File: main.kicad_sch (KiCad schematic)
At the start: 80 parts, among them SW1 Kailh-Choc, SW10 Kailh-Choc, SW11 Kailh-Choc, SW12 Kailh-Choc, SW13 Kailh-Choc, SW14 Kailh-Choc, SW15 Kailh-Choc, SW16 Kailh-Choc, SW17 Kailh-Choc, SW18 Kailh-Choc, SW19 Kailh-Choc, SW2 Kailh-Choc, SW20 Kailh-Choc, SW21 Kailh-Choc, SW22 Kailh-Choc, SW23 Kailh-Choc, SW24 Kailh-Choc, SW25 Kailh-Choc, SW26 Kailh-Choc, SW27 Kailh-Choc, SW28 Kailh-Choc, SW29 Kailh-Choc, SW3 Kailh-Choc, SW30 Kailh-Choc, SW31 Kailh-Choc, SW32 Kailh-Choc, SW33 Kailh-Choc, SW34 Kailh-Choc, SW4 Kailh-Choc, SW5 Kailh-Choc, SW6 Kailh-Choc, SW7 Kailh-Choc, SW8 Kailh-Choc, SW9 Kailh-Choc, U1 nice_nano, U2 nice_nano

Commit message: Use local library only
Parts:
- Bat+0, Bat+1, BatGND0, BatGND1: footprint * duckyb-collection:1pin_conn -> urchin-footprints:1pin_Battery
- D1, D10, D11, D12, D13, D14, D15, D16, D17, D18, D19, D2, D20, D21, D22, D23, D24, D25, D26, D27, D28, D29, D3, D30, D31, D32, D33, D34, D4, D5, D6, D7, D8, D9: footprint * duckyb-collection:D_SMD_TH -> urchin-footprints:SMD_Diode_Tiny
- Display1, Display2: footprint * duckyb-collection:nice_view -> urchin-footprints:nice_view
- RSW0, RSW1: footprint * duckyb-collection:SW_RESET -> urchin-footprints:SW_RESET
- SW1, SW10, SW11, SW12, SW13, SW14, SW15, SW16, SW17, SW18, SW19, SW2, SW20, SW21, SW22, SW23, SW24, SW25, SW26, SW27, SW28, SW29, SW3, SW30, SW31, SW32, SW33, SW34, SW4, SW5, SW6, SW7, SW8, SW9: footprint * duckyb-collection:SW_Hotswap_Kailh_Choc_V1_tweaked -> urchin-footprints:SW_Hotswap_Kailh_Choc_V1_tweaked
- SW_POWER0, SW_POWER1: footprint * duckyb-collection:SPDT_C128955 -> urchin-footprints:smt-slider-switch
- U1, U2: footprint * duckyb-collection:nice_nano -> urchin-footprints:nice_nano

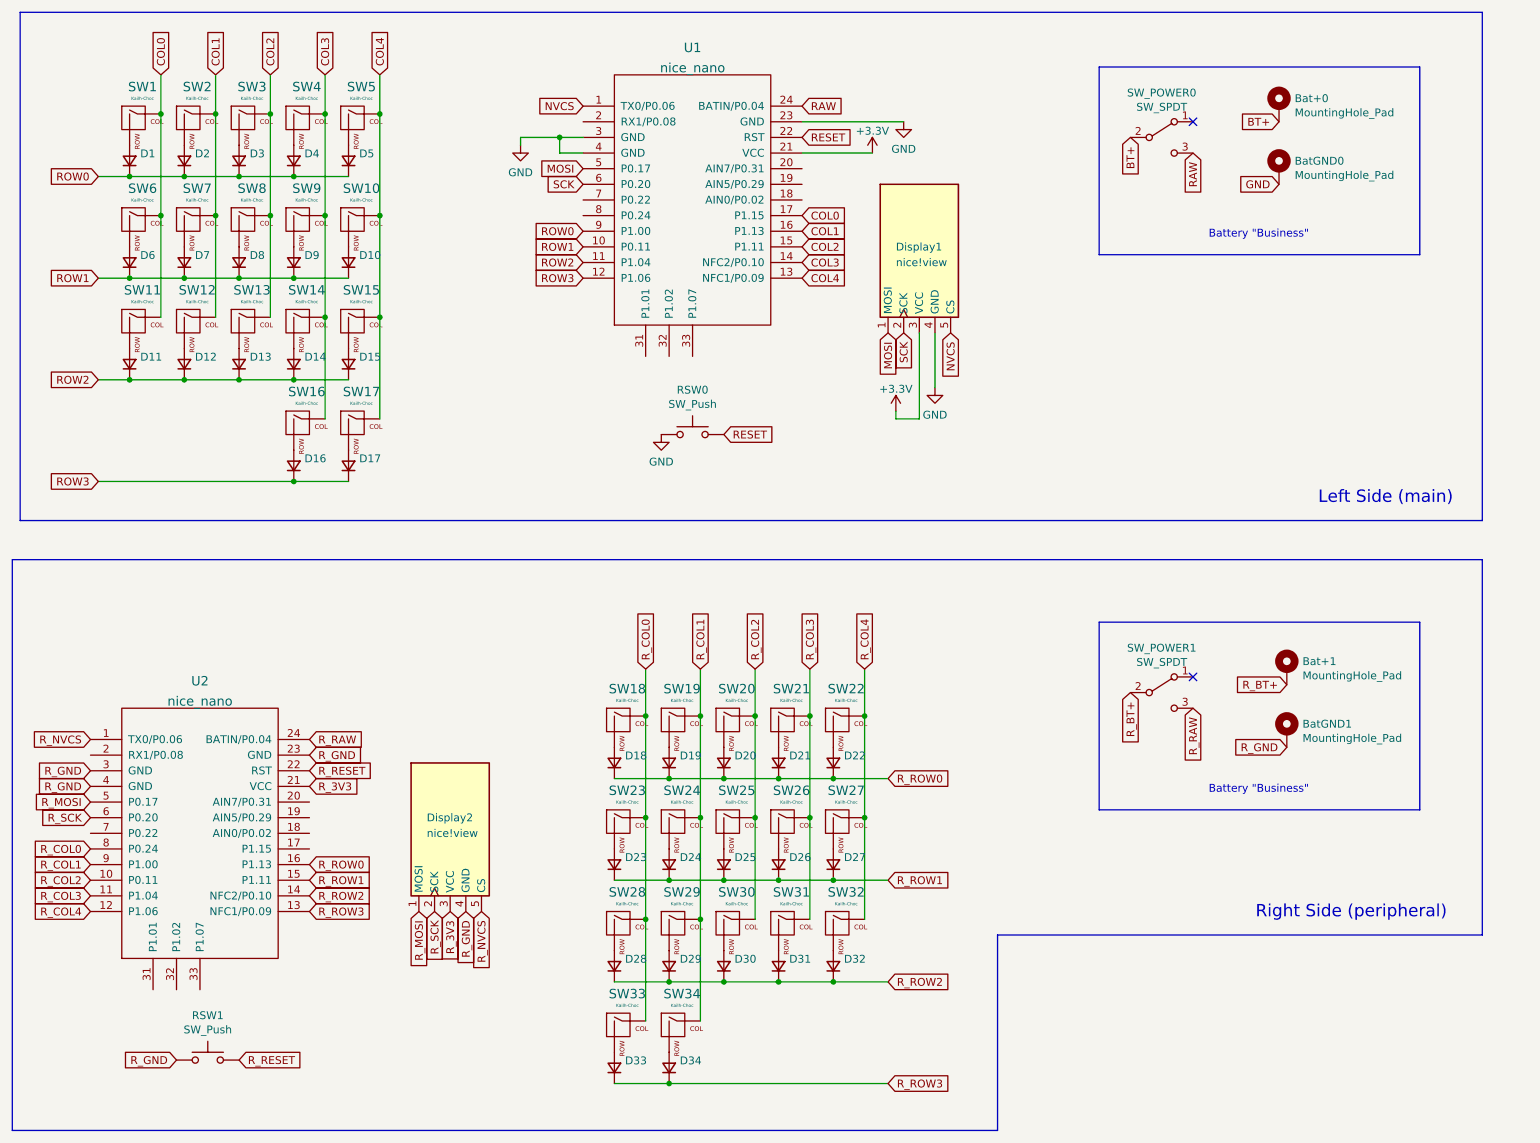
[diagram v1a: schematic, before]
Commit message: Update to Kicad 8, improve routing, fix DRC
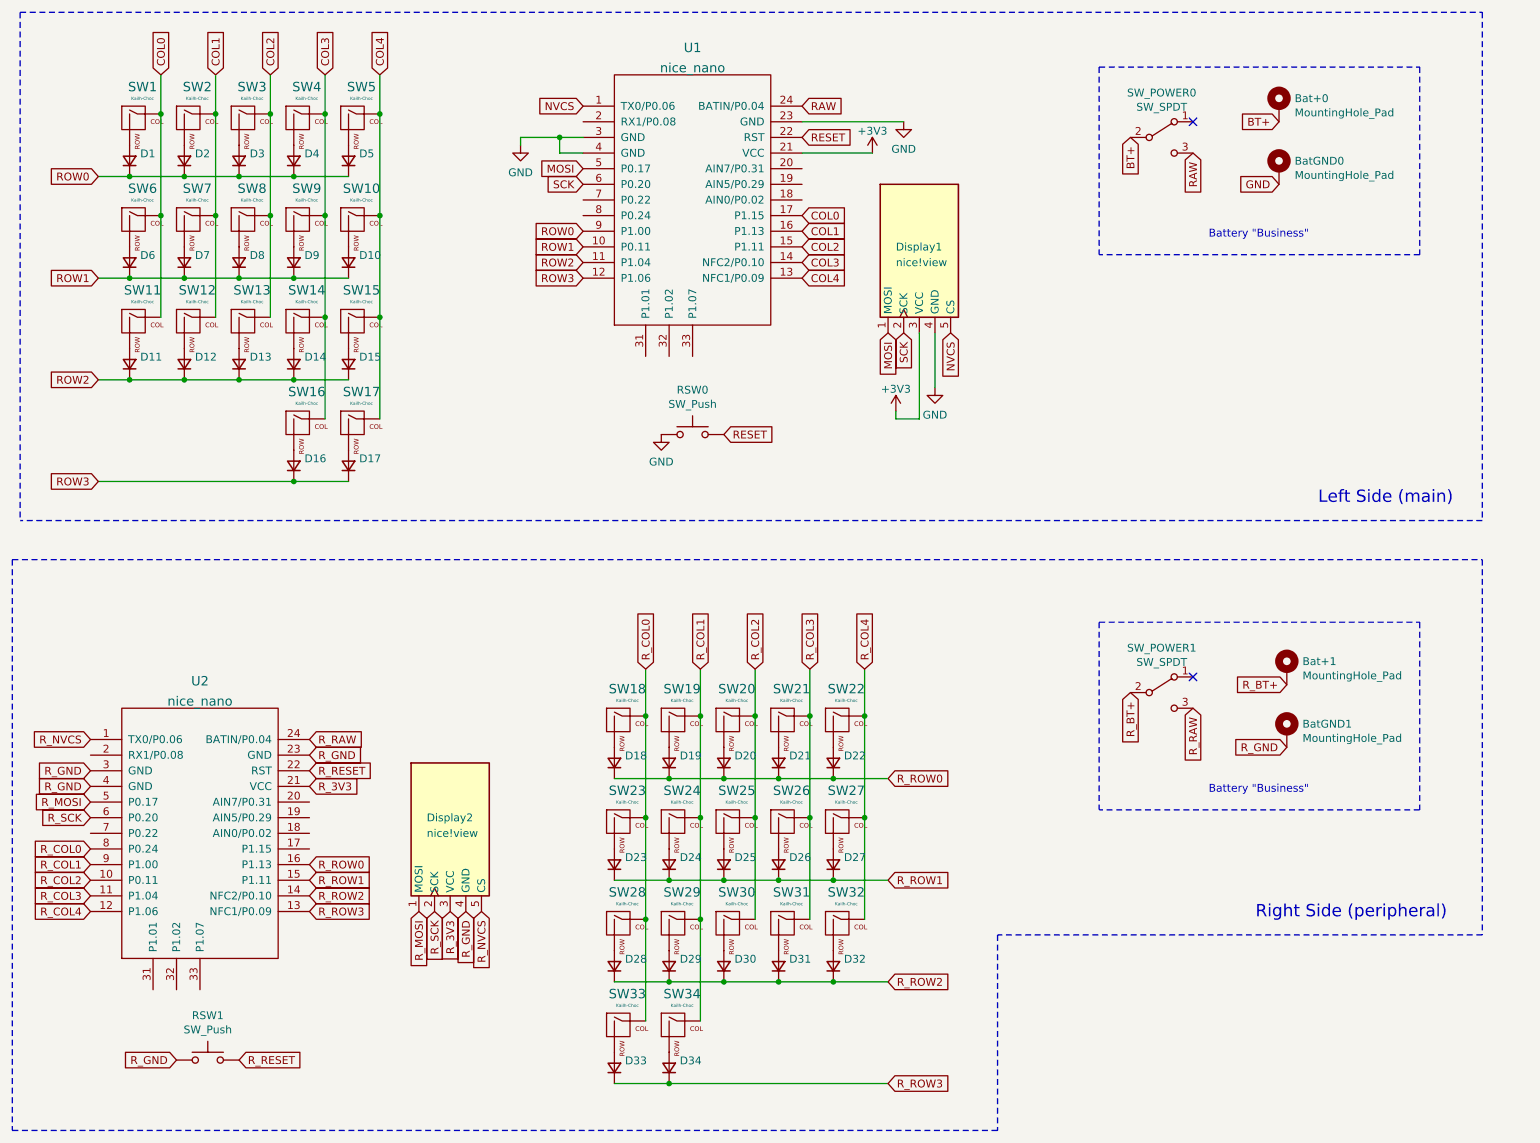
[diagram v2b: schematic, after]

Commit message: Revert "Update to Kicad 8, improve routing, fix DRC"
This reverts commit f1fb744aeca04b057ba63b33434fe6fbb2a0fd1e.
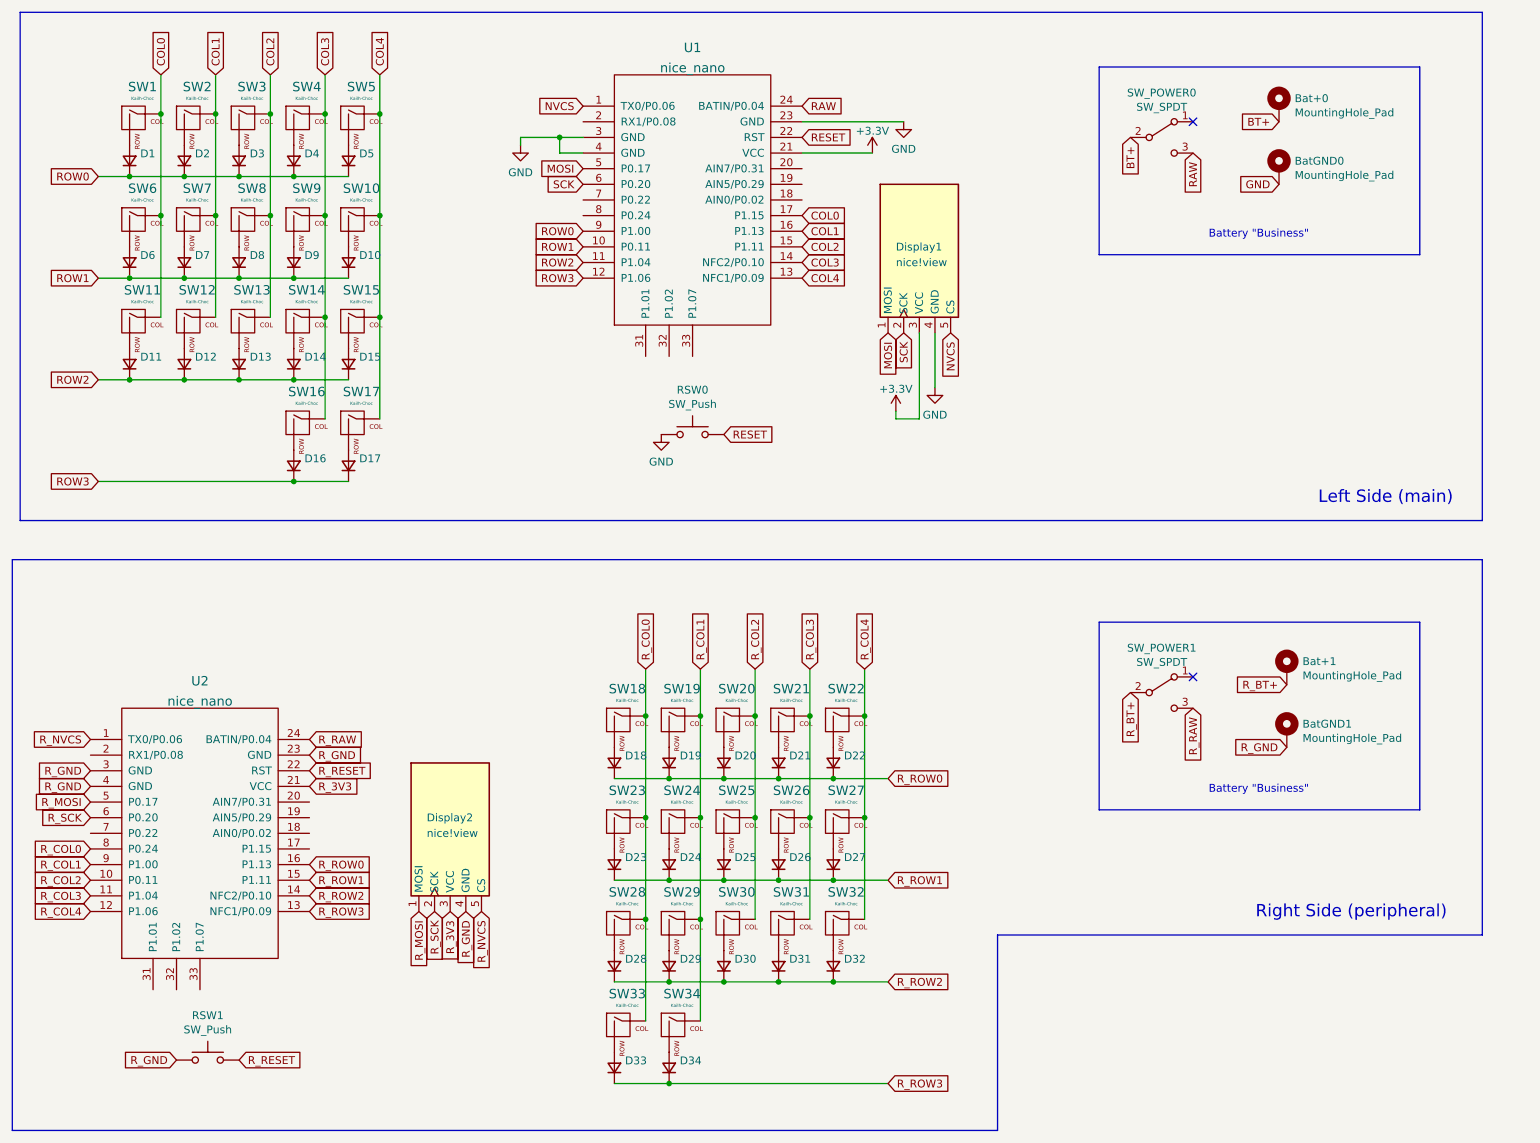
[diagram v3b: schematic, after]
